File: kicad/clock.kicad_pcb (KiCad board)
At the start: 4 copper layers, 87 x 38 mm, 56 parts, among them P1 CONN_01X03, SW1 SWITCH_MIN, SW2 SWITCH_HR, U1 74LS90, U10 74LS247, U11 74LS73, U2 74LS90, U3 MAX6817, U4 74LS90, U5 74LS247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

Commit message: Update netlist after changing resistor values from 220Ohms to 150Ohms
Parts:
- R12, R13: value 220Ω -> 150Ω
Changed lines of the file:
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@@
       (effects (font (size 0.75 0.75) (thickness 0.15)) (justify mirror))
     )
-    (fp_text value 220Ω (at 0 -2.1 270) (layer B.Fab) hide
+    (fp_text value 150Ω (at 0 -2.1 270) (layer B.Fab) hide
       (effects (font (size 1 1) (thickness 0.15)) (justify mirror))
     )
@@
       (effects (font (size 0.75 0.75) (thickness 0.15)) (justify mirror))
     )
-    (fp_text value 220Ω (at 0 -2.1 270) (layer B.Fab) hide
+    (fp_text value 150Ω (at 0 -2.1 270) (layer B.Fab) hide
       (effects (font (size 1 1) (thickness 0.15)) (justify mirror))
     )

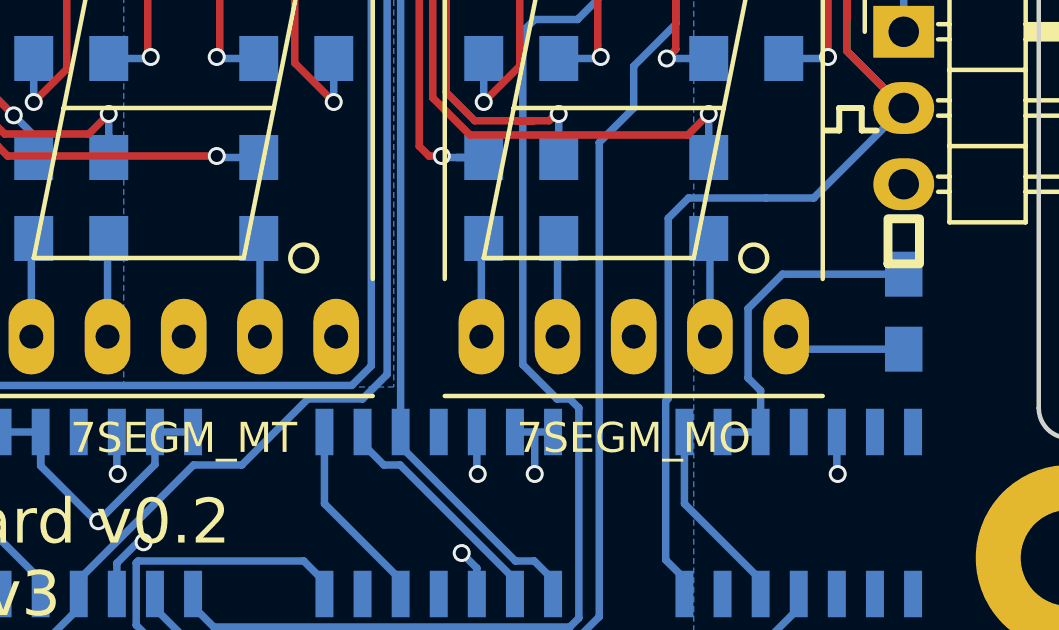
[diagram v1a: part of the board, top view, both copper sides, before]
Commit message: Close up some copper pour gaps
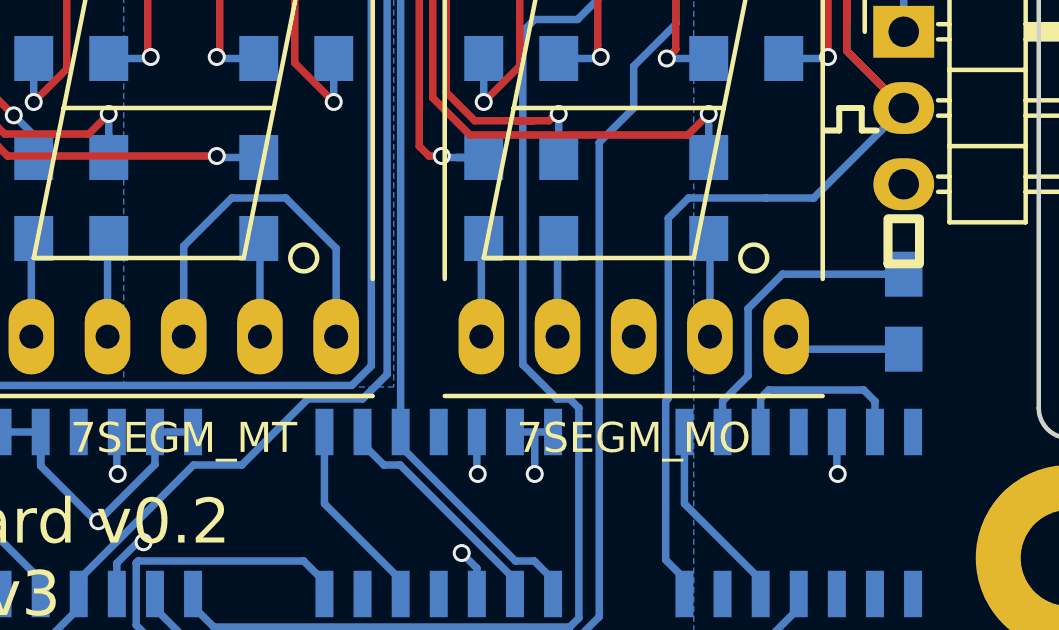
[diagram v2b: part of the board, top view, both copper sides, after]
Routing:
- net VCC: track 115.1 -> 127.5 mm
- net GND: track 42.2 -> 47.4 mm
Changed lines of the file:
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@@
     (thickness 1.6)
     (drawings 27)
-    (tracks 990)
+    (tracks 999)
     (zones 0)
     (modules 56)
@@
   )
   (layers
-    (0 F.Cu signal)
-    (1 In1.Cu signal)
-    (2 In2.Cu signal)
+    (0 F.Cu signal hide)
+    (1 In1.Cu signal hide)
+    (2 In2.Cu signal hide)
     (31 B.Cu signal)
     (32 B.Adhes user)
@@
     (effects (font (size 1.5 1.5) (thickness 0.3)))
   )
+  (segment (start 168.4 99) (end 170.08 100.68) (width 0.25) (layer B.Cu) (net 1))
+  (segment (start 170.08 100.68) (end 170.08 103.62) (width 0.25) (layer B.Cu) (net 1))
+  (segment (start 166.6 99) (end 168.4 99) (width 0.25) (layer B.Cu) (net 1))
+  (segment (start 165 100.6) (end 166.6 99) (width 0.25) (layer B.Cu) (net 1))
+  (segment (start 165 103.62) (end 165 100.6) (width 0.25) (layer B.Cu) (net 1))
   (segment (start 126.905 112.2) (end 126.905 112.675) (width 0.25) (layer B.Cu) (net 1))
   (segment (start 126.905 112.675) (end 126.279999 113.300001) (width 0.25) (layer B.Cu) (net 1))
@@
   (segment (start 186.77 108.17) (end 186.8 108.2) (width 0.25) (layer B.Cu) (net 1))
   (via (at 186.8 108.2) (size 0.6) (drill 0.4) (layers F.Cu B.Cu) (net 1))
+  (segment (start 184.23 106.8) (end 184.23 105.67) (width 0.25) (layer B.Cu) (net 2))
+  (segment (start 184.23 105.67) (end 184.5 105.4) (width 0.25) (layer B.Cu) (net 2))
+  (segment (start 188.04 105.775) (end 188.04 106.8) (width 0.25) (layer B.Cu) (net 2))
+  (segment (start 184.5 105.4) (end 187.665 105.4) (width 0.25) (layer B.Cu) (net 2))
+  (segment (start 187.665 105.4) (end 188.04 105.775) (width 0.25) (layer B.Cu) (net 2))
+  (segment (start 182.96 106.8) (end 182.96 105.775) (width 0.25) (layer B.Cu) (net 2))
+  (segment (start 182.96 105.775) (end 183.810486 104.924514) (width 0.25) (layer B.Cu) (net 2))
+  (segment (start 183.810486 104.924514) (end 183.810486 102.685615) (width 0.25) (layer B.Cu) (net 2))
+  (segment (start 183.810486 102.685615) (end 184.956101 101.54) (width 0.25) (layer B.Cu) (net 2))
+  (segment (start 184.956101 101.54) (end 189 101.54) (width 0.25) (layer B.Cu) (net 2))
   (segment (start 153.2 92.2) (end 153.2 92.9) (width 0.25) (layer B.Cu) (net 2))
   (segment (start 153.75 91.65) (end 153.2 92.2) (width 0.25) (layer B.Cu) (net 2))
   (segment (start 153.75 91.5) (end 153.75 91.65) (width 0.25) (layer B.Cu) (net 2))
   (via (at 153.2 92.9) (size 0.6) (drill 0.4) (layers F.Cu B.Cu) (net 2))
-  (segment (start 183.810486 102.685615) (end 184.956101 101.54) (width 0.25) (layer B.Cu) (net 2))
-  (segment (start 184.956101 101.54) (end 189 101.54) (width 0.25) (layer B.Cu) (net 2))
-  (segment (start 183.810486 102.685615) (end 183.810486 105) (width 0.25) (layer B.Cu) (net 2))
-  (segment (start 184.23 106.8) (end 184.23 105.419514) (width 0.25) (layer B.Cu) (net 2))
-  (segment (start 184.23 105.419514) (end 183.810486 105) (width 0.25) (layer B.Cu) (net 2))
   (segment (start 176.797168 85.2) (end 176.787319 85.209849) (width 0.25) (layer B.Cu) (net 2))
   (segment (start 177.555 85.2) (end 176.797168 85.2) (width 0.25) (layer B.Cu) (net 2))
@@
   (via (at 174.265558 110.834442) (size 0.6) (drill 0.4) (layers F.Cu B.Cu) (net 2))
   (segment (start 184.23 107.275) (end 184.23 106.8) (width 0.25) (layer B.Cu) (net 2))
-  (segment (start 182.96 106.8) (end 184.23 106.8) (width 0.25) (layer B.Cu) (net 2))
   (segment (start 176.7 106.8) (end 177.31 106.8) (width 0.25) (layer B.Cu) (net 2))
   (segment (start 176.04 106.8) (end 176.7 106.8) (width 0.25) (layer B.Cu) (net 2))

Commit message: Brint input D of U8 to GND
Was floating
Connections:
- U8 pad 6: Net-(U8-Pad6) -> GND
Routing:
- net GND: track 47.4 -> 48.8 mm, vias 13 -> 14
- net VCC: track 127.5 -> 128.5 mm
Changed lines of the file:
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@@
 (kicad_pcb (version 4) (host pcbnew 4.0.4-1.fc25-product)
   (general
-    (links 179)
+    (links 180)
     (no_connects 0)
     (area 105.982857 73 204.017143 119.000001)
     (thickness 1.6)
     (drawings 27)
-    (tracks 999)
+    (tracks 1002)
     (zones 0)
     (modules 56)
-    (nets 89)
+    (nets 88)
   )
   (page A4)
@@
   )
   (layers
-    (0 F.Cu signal hide)
-    (1 In1.Cu signal hide)
-    (2 In2.Cu signal hide)
+    (0 F.Cu signal)
+    (1 In1.Cu signal)
+    (2 In2.Cu signal)
     (31 B.Cu signal)
     (32 B.Adhes user)
@@
   (net 85 "Net-(U7-Pad12)")
   (net 86 "Net-(U8-Pad4)")
-  (net 87 "Net-(U8-Pad6)")
-  (net 88 "Net-(R4-Pad2)")
+  (net 87 "Net-(R4-Pad2)")
   (net_class Default "This is the default net class."
     (clearance 0.16)
@@
     (add_net "Net-(U7-Pad3)")
     (add_net "Net-(U8-Pad4)")
-    (add_net "Net-(U8-Pad6)")
     (add_net "Net-(U9-Pad15)")
     (add_net VCC)
@@
       (net 1 VCC) (solder_mask_margin 0.07))
     (pad 6 smd rect (at 1.905 -2.7 180) (size 0.6 1.55) (layers B.Cu B.Paste B.Mask)
-      (net 87 "Net-(U8-Pad6)") (solder_mask_margin 0.07))
+      (net 2 GND) (solder_mask_margin 0.07))
     (pad 7 smd rect (at 3.175 -2.7 180) (size 0.6 1.55) (layers B.Cu B.Paste B.Mask)
       (net 71 /mti0) (solder_mask_margin 0.07))
@@
       (net 9 /ht))
     (pad 2 smd rect (at 1.35 0 270) (size 1.5 1.3) (layers B.Cu B.Paste B.Mask)
-      (net 88 "Net-(R4-Pad2)"))
+      (net 87 "Net-(R4-Pad2)"))
     (model Resistors_SMD.3dshapes/R_0805_HandSoldering.wrl
       (at (xyz 0 0 0))
@@
       (net 1 VCC))
     (pad 4 thru_hole oval (at 2.54 7.62) (size 1.524 2.524) (drill 0.8) (layers *.Cu *.Mask F.SilkS)
-      (net 88 "Net-(R4-Pad2)"))
+      (net 87 "Net-(R4-Pad2)"))
     (pad 5 thru_hole oval (at 5.08 7.62) (size 1.524 2.524) (drill 0.8) (layers *.Cu *.Mask F.SilkS)
       (net 1 VCC))
@@
     (effects (font (size 1.5 1.5) (thickness 0.3)))
   )
+  (segment (start 159.15 83.214998) (end 158.2 84.164998) (width 0.25) (layer B.Cu) (net 1))
+  (segment (start 160.404998 83.214998) (end 159.15 83.214998) (width 0.25) (layer B.Cu) (net 1))
+  (segment (start 161.365 84.175) (end 160.404998 83.214998) (width 0.25) (layer B.Cu) (net 1))
+  (segment (start 158.2 84.164998) (end 158.2 84.5) (width 0.25) (layer B.Cu) (net 1))
+  (segment (start 161.365 85.2) (end 161.365 84.175) (width 0.25) (layer B.Cu) (net 1))
   (segment (start 168.4 99) (end 170.08 100.68) (width 0.25) (layer B.Cu) (net 1))
   (segment (start 170.08 100.68) (end 170.08 103.62) (width 0.25) (layer B.Cu) (net 1))
@@
   (segment (start 153.6 97.224264) (end 153.6 96.8) (width 0.25) (layer B.Cu) (net 1))
   (segment (start 153.6 100.85) (end 153.6 97.224264) (width 0.25) (layer B.Cu) (net 1))
-  (segment (start 161.365 85.2) (end 161.365 84.665) (width 0.25) (layer B.Cu) (net 1))
-  (segment (start 161.365 84.665) (end 160.799999 84.099999) (width 0.25) (layer B.Cu) (net 1))
   (segment (start 156.35 88) (end 157.090002 88) (width 0.25) (layer B.Cu) (net 1))
   (segment (start 157.090002 88) (end 157.466933 87.623069) (width 0.25) (layer B.Cu) (net 1))
@@
   (segment (start 158.2 86.103762) (end 158.2 84.5) (width 0.25) (layer B.Cu) (net 1))
   (segment (start 158.2 84.5) (end 158.2 84.2) (width 0.25) (layer B.Cu) (net 1))
-  (segment (start 158.2 84.164998) (end 158.2 84.5) (width 0.25) (layer B.Cu) (net 1))
-  (segment (start 160.799999 84.099999) (end 158.264999 84.099999) (width 0.25) (layer B.Cu) (net 1))
-  (segment (start 158.264999 84.099999) (end 158.2 84.164998) (width 0.25) (layer B.Cu) (net 1))
   (segment (start 156.25 91.5) (end 156.1 91.5) (width 0.25) (layer B.Cu) (net 1))
   (segment (start 156.1 91.5) (end 155 92.6) (width 0.25) (layer B.Cu) (net 1))
@@
   (segment (start 186.77 108.17) (end 186.8 108.2) (width 0.25) (layer B.Cu) (net 1))
   (via (at 186.8 108.2) (size 0.6) (drill 0.4) (layers F.Cu B.Cu) (net 1))
+  (segment (start 160.095 85.2) (end 160.095 83.805) (width 0.25) (layer B.Cu) (net 2))
+  (segment (start 160.095 83.805) (end 160.1 83.8) (width 0.25) (layer B.Cu) (net 2))
+  (via (at 160.1 83.8) (size 0.6) (drill 0.4) (layers F.Cu B.Cu) (net 2))
   (segment (start 184.23 106.8) (end 184.23 105.67) (width 0.25) (layer B.Cu) (net 2))
   (segment (start 184.23 105.67) (end 184.5 105.4) (width 0.25) (layer B.Cu) (net 2))
@@
   (segment (start 130.150001 111.099999) (end 134.334999 111.099999) (width 0.25) (layer B.Cu) (net 85))
   (segment (start 134.96 111.725) (end 134.96 112.2) (width 0.25) (layer B.Cu) (net 85) (status 30))
-  (segment (start 132.54 103.62) (end 132.54 100.39) (width 0.25) (layer B.Cu) (net 88) (status 30))
-  (segment (start 132.54 100.39) (end 132.5 100.35) (width 0.25) (layer B.Cu) (net 88) (status 30))
+  (segment (start 132.54 103.62) (end 132.54 100.39) (width 0.25) (layer B.Cu) (net 87) (status 30))
+  (segment (start 132.54 100.39) (end 132.5 100.35) (width 0.25) (layer B.Cu) (net 87) (status 30))
   (zone (net 2) (net_name GND) (layer F.Cu) (hatch edge 0.508)
     (connect_pads (clearance 0.508))
@@
       )
     )
+  )
+  (zone (net 0) (net_name "") (layer F.Cu) (hatch full 0.508)
+    (connect_pads (clearance 0.508))
+    (min_thickness 0.254)
+    (keepout (tracks allowed) (vias allowed) (copperpour not_allowed))
+    (fill (arc_segments 16) (thermal_gap 0.508) (thermal_bridge_width 0.508))
+    (polygon
+      (pts
+        (xy 160.5 83.5) (xy 159.75 83.5) (xy 159.75 84.25) (xy 160.5 84.25)
+      )
+    )

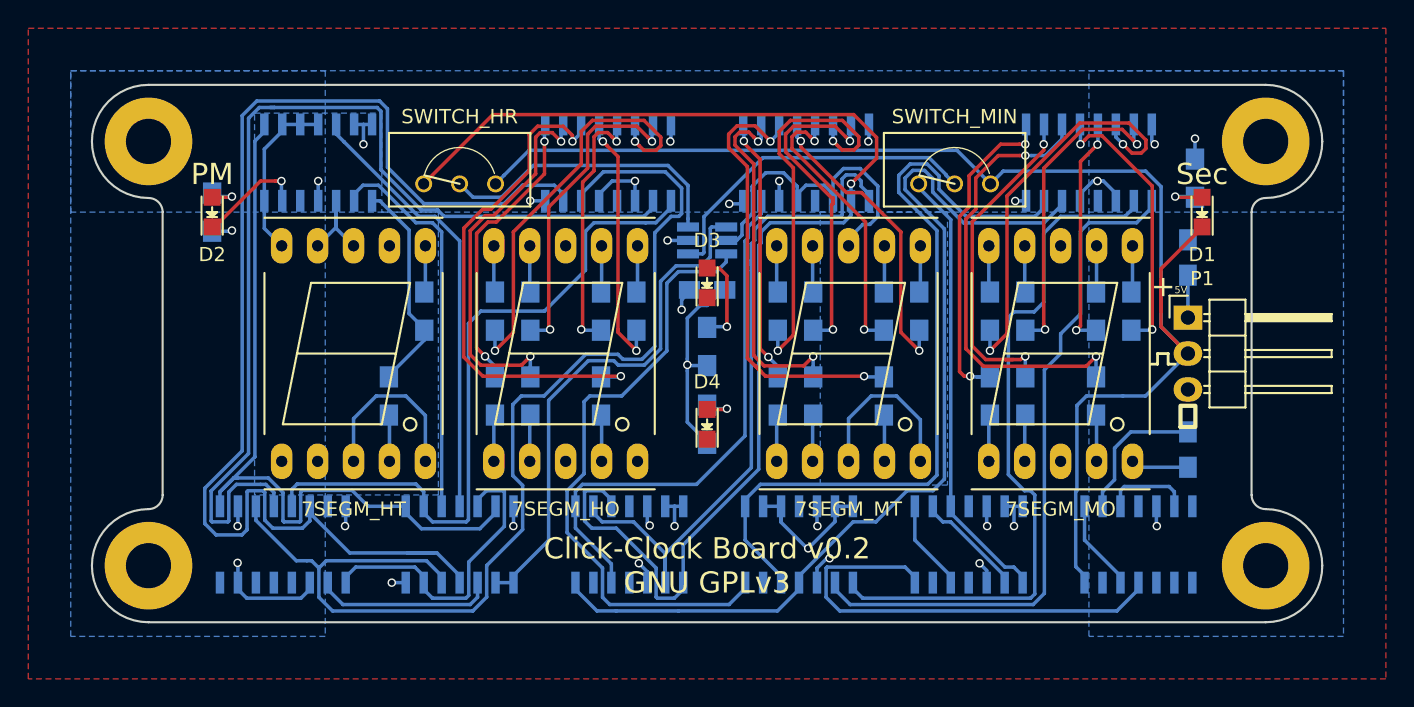
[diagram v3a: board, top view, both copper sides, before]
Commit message: Swap pin 1 and 3 of the SPDT push button footprint and update layout accordingly
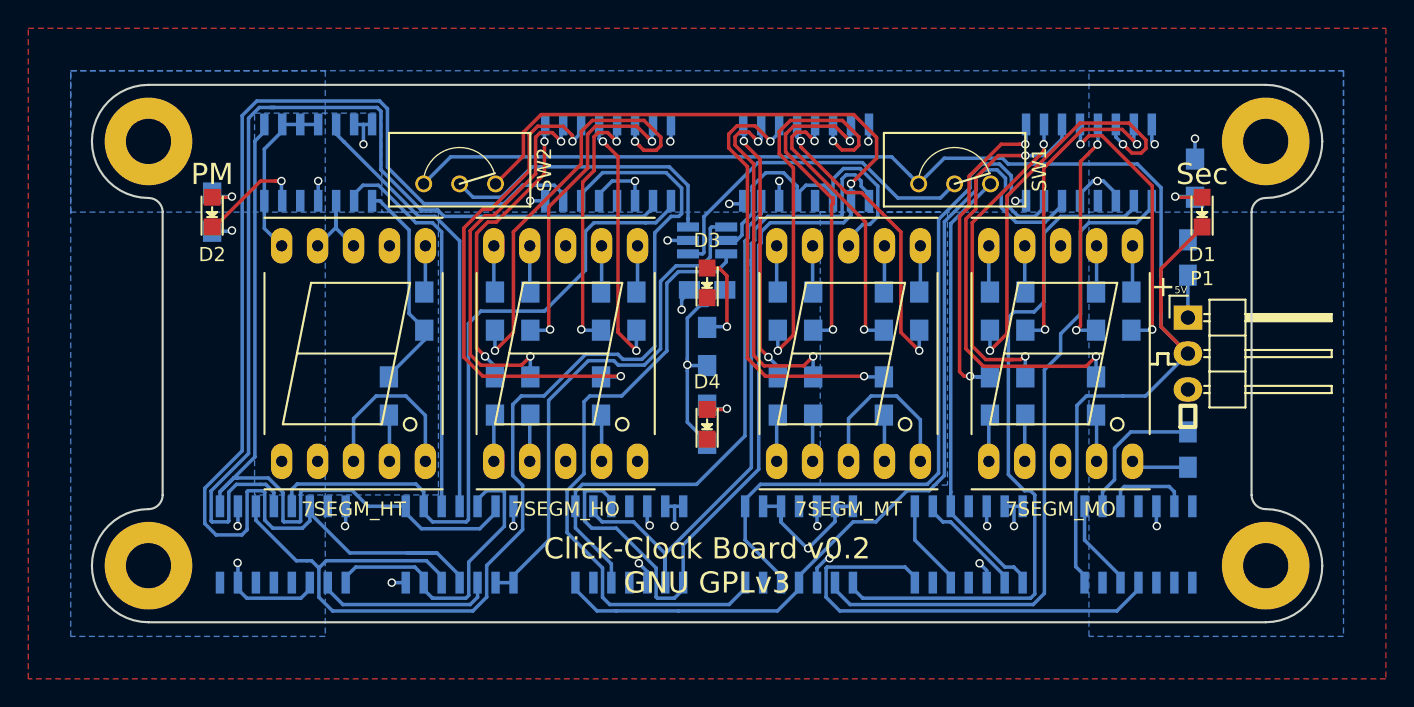
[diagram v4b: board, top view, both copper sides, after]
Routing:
- net /osc: track 98.4 -> 104.3 mm
- net /moi3: track 68.3 -> 64.0 mm
- net /moi0: track 57.0 -> 52.8 mm
- net /mti2: track 91.8 -> 87.7 mm
- net Net-(SW1-Pad2): track 23.9 -> 24.5 mm

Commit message: Further optimize the routing
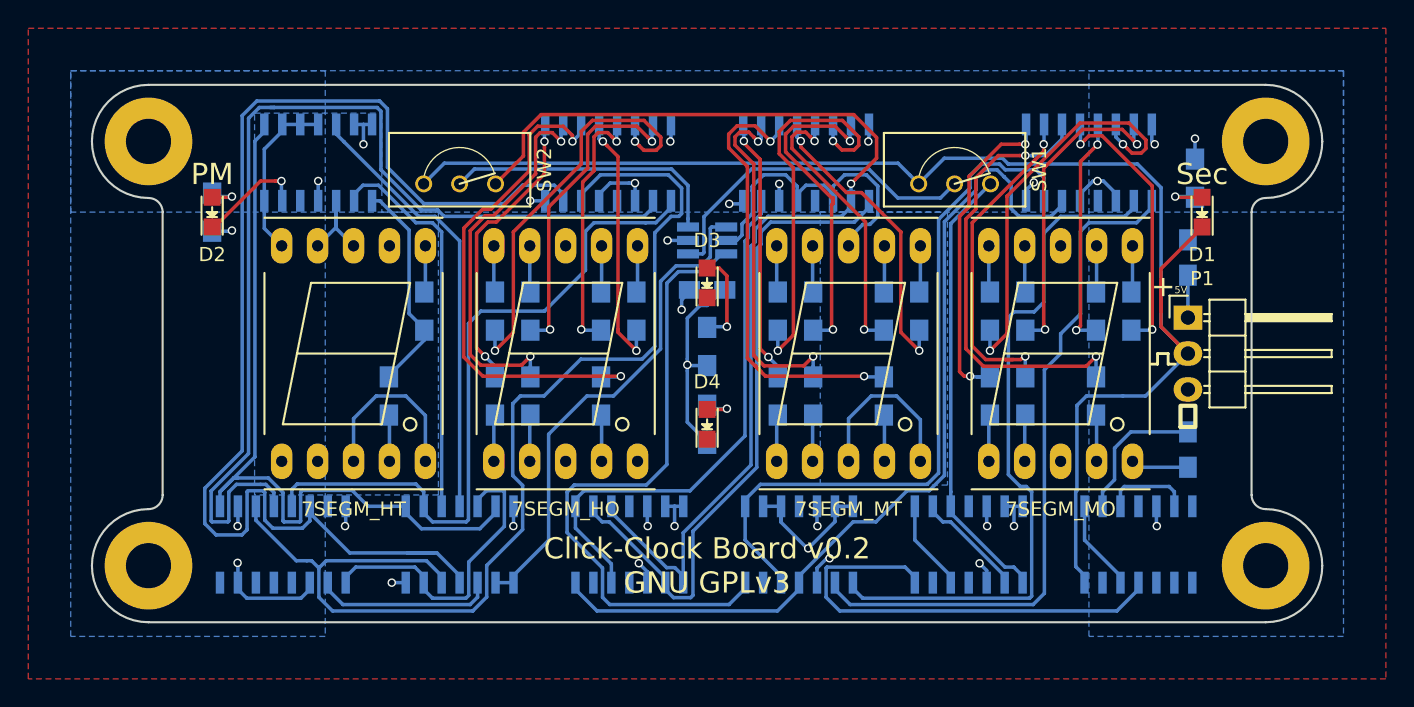
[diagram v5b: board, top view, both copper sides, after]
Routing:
- net /mti2: track 87.7 -> 80.1 mm
- net /mti1: track 49.7 -> 47.5 mm
- net /moi0: track 52.8 -> 50.9 mm
- net Net-(U3-Pad4): track 37.1 -> 35.4 mm
- net Net-(U3-Pad6): track 44.6 -> 45.9 mm
- net VCC: track 128.5 -> 127.5 mm
- net /moi3: track 64.0 -> 63.0 mm
- net Net-(SW2-Pad2): track 20.9 -> 20.0 mm
- net GND: track 48.8 -> 49.3 mm
